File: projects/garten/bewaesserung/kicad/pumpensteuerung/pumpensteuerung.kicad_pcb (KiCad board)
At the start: 2 copper layers, 100 x 85 mm, 26 parts, among them J1 Screw_Terminal_01x03, J2 Screw_Terminal_01x02, J4 Screw_Terminal_01x03, J5 Screw_Terminal_01x03, K2 SANYOU_SRD_Form_C, K3 SANYOU_SRD_Form_C, K4 SANYOU_SRD_Form_C, Q1 2N3904, Q2 2N3904, Q3 2N3904

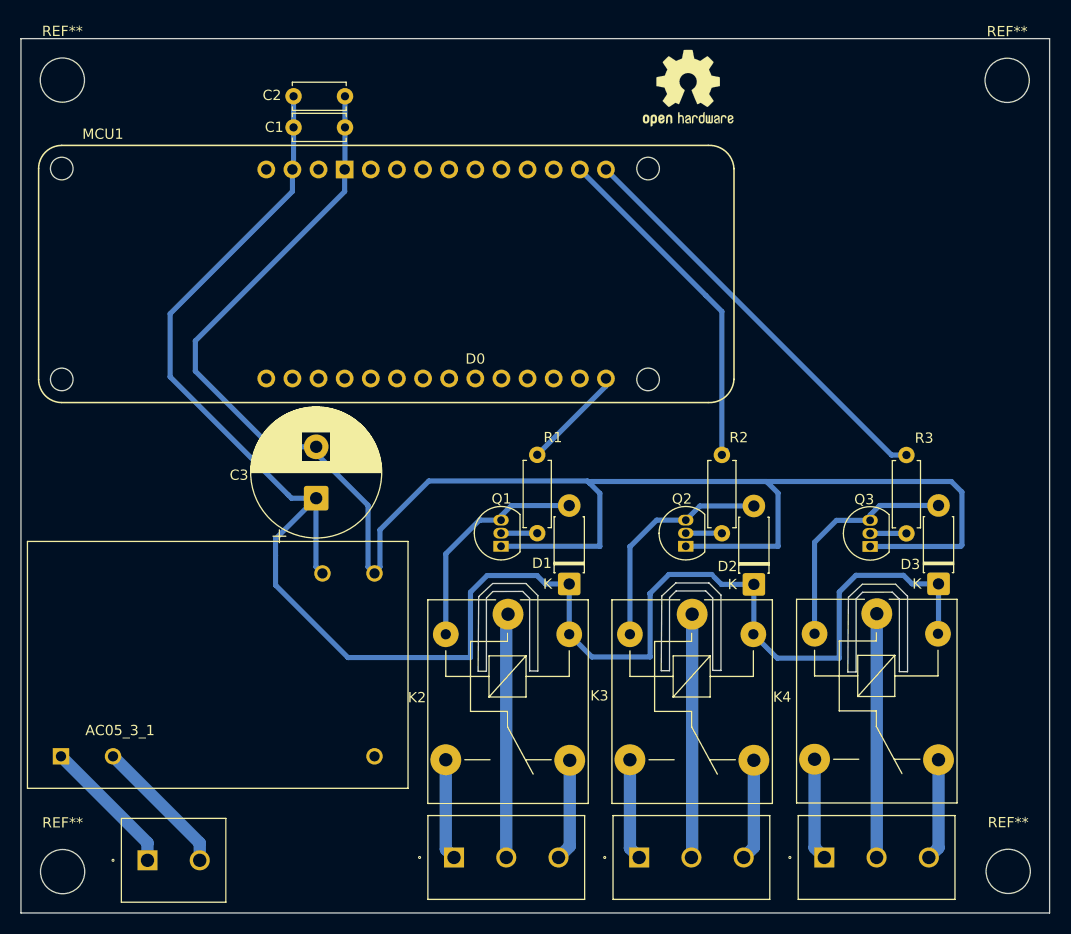
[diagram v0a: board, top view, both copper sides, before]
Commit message: [garten/bewaesserung] change powersupply from 230VAC to 24VDC
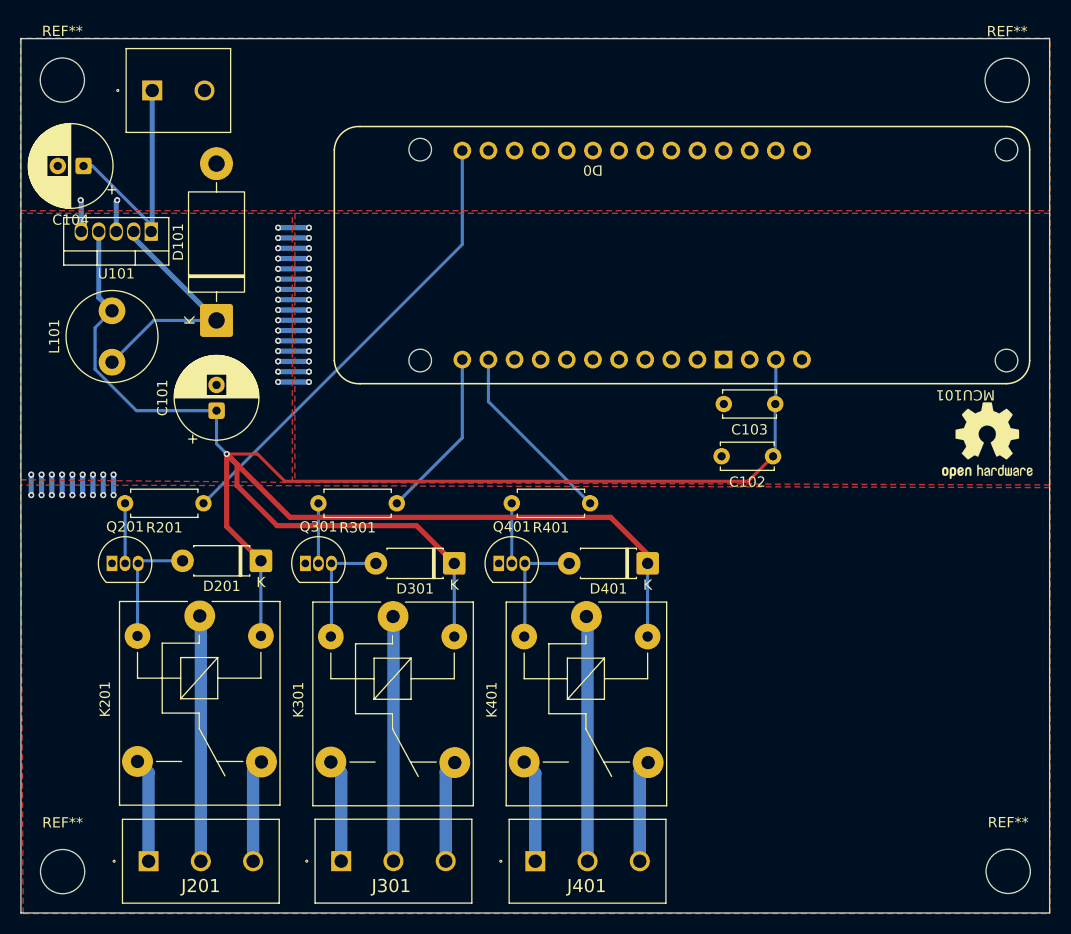
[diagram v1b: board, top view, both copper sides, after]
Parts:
- removed AC05_3_1: ~, AZFootprints:AZ_PSU_Module
- removed C1: 10000pF 100V 10% Y5P 5mm, Capacitor_THT:C_Disc_D5.0mm_W2.5mm_P5.00mm
- removed C2: 0.1uF 500V +80/-20%, Capacitor_THT:C_Disc_D5.0mm_W2.5mm_P5.00mm
- removed C3: 1000 µF, 25 V, 105°C, low ESR, 12,5 x 20 mm, RM 5, Capacitor_THT:CP_Radial_D12.5mm_P5.00mm
- removed D1, D2, D3: 1N4007, Diode_THT:D_DO-41_SOD81_P7.62mm_Horizontal
- removed J1, J4, J5: Screw_Terminal_01x03, PhoenixContact:MKDSN 1,5_3-5,08
- removed J2: Screw_Terminal_01x02, PhoenixContact:MKDSN 1,5_2-5,08
- removed K2, K3, K4: SANYOU_SRD_Form_C, Relay_THT:Relay_SPDT_SANYOU_SRD_Series_Form_C
- removed MCU1: Arduino_MKR_WAN_1310_Socket, PCM_arduino-library:Arduino_MKR_FOX_1200_Socket
- removed Q1, Q2, Q3: 2N3904, Package_TO_SOT_THT:TO-92_Inline
- removed R1, R2, R3: 220 OHM 0.6W 1% AXIAL, Resistor_THT:R_Axial_DIN0207_L6.3mm_D2.5mm_P7.62mm_Horizontal
- added C101: 330µF, Capacitor_THT:CP_Radial_D8.0mm_P2.50mm, F.Cu at (69.5, 85.2)
- added C102: 0.1uF 500V +80/-20%, Capacitor_THT:C_Disc_D5.0mm_W2.5mm_P5.00mm, F.Cu at (123.6, 89.6)
- added C103: 10000pF 100V 10% Y5P 5mm, Capacitor_THT:C_Disc_D5.0mm_W2.5mm_P5.00mm, F.Cu at (123.8, 84.5)
- added C104: 330µF, Capacitor_THT:CP_Radial_D8.0mm_P2.50mm, F.Cu at (56.6, 61.4)
- added D101: 1N5822, Diode_THT:D_DO-201AD_P15.24mm_Horizontal, F.Cu at (69.5, 76.4)
- added D201: 1N4007, Diode_THT:D_DO-41_SOD81_P7.62mm_Horizontal, F.Cu at (73.8, 99.8)
- added D301: 1N4007, Diode_THT:D_DO-41_SOD81_P7.62mm_Horizontal, F.Cu at (92.6, 100.0)
- added D401: 1N4007, Diode_THT:D_DO-41_SOD81_P7.62mm_Horizontal, F.Cu at (111.4, 100.0)
- added J101: Screw_Terminal_01x02, PhoenixContact:MKDSN 1,5_2-5,08, F.Cu at (63.3, 54.0)
- added J201: Screw_Terminal_01x03, PhoenixContact:MKDSN 1,5_3-5,08, F.Cu at (62.9, 129.0)
- added J301: Screw_Terminal_01x03, PhoenixContact:MKDSN 1,5_3-5,08, F.Cu at (81.6, 129.0)
- added J401: Screw_Terminal_01x03, PhoenixContact:MKDSN 1,5_3-5,08, F.Cu at (100.5, 129.0)
- added K201: SANYOU_SRD_Form_C, Relay_THT:Relay_SPDT_SANYOU_SRD_Series_Form_C, F.Cu at (67.9, 105.1)
- added K301: SANYOU_SRD_Form_C, Relay_THT:Relay_SPDT_SANYOU_SRD_Series_Form_C, F.Cu at (86.7, 105.2)
- added K401: SANYOU_SRD_Form_C, Relay_THT:Relay_SPDT_SANYOU_SRD_Series_Form_C, F.Cu at (105.5, 105.2)
- added L101: 330µH, Inductor_THT:L_Radial_D8.7mm_P5.00mm_Fastron_07HCP, F.Cu at (59.4, 80.5)
- added MCU101: Arduino_MKR_WAN_1310_Socket, PCM_arduino-library:Arduino_MKR_FOX_1200_Socket, F.Cu at (146.3, 80.3)
- added Q201: 2N3904, Package_TO_SOT_THT:TO-92_Inline, F.Cu at (59.4, 100.0)
- added Q301: 2N3904, Package_TO_SOT_THT:TO-92_Inline, F.Cu at (78.1, 100.0)
- added Q401: 2N3904, Package_TO_SOT_THT:TO-92_Inline, F.Cu at (96.9, 100.0)
- added R201: 1K OHM 1/2W 1% AXIAL, Resistor_THT:R_Axial_DIN0207_L6.3mm_D2.5mm_P7.62mm_Horizontal, F.Cu at (68.2, 94.2)
- added R301: 1K OHM 1/2W 1% AXIAL, Resistor_THT:R_Axial_DIN0207_L6.3mm_D2.5mm_P7.62mm_Horizontal, F.Cu at (87.0, 94.2)
- added R401: 1K OHM 1/2W 1% AXIAL, Resistor_THT:R_Axial_DIN0207_L6.3mm_D2.5mm_P7.62mm_Horizontal, F.Cu at (105.8, 94.2)
- added U101: LM2575-5.0BT, Package_TO_SOT_THT:TO-220-5_Vertical, F.Cu at (63.2, 67.8)
- moved REF** 44.9 mm to (144.4, 88.1)
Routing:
- net /-5V: track 175.4 -> 0.00 mm
- net GND: track 14.0 -> 72.2 mm, vias 0 -> 52
- net /Hauptrelais: track 10.2 -> 44.7 mm
- net /+5V: track 177.2 -> 204.4 mm, vias 0 -> 1
- net Net-(D101-K): track 0.00 -> 24.1 mm
- net Net-(D3-A): track 22.8 -> 0.00 mm
- net /Poolrelais: track 40.7 -> 18.1 mm
- net Net-(D2-A): track 22.2 -> 0.00 mm
- net Net-(D1-A): track 22.0 -> 0.00 mm
- net /Bewaesserungsrelais: track 34.1 -> 16.6 mm
- net Net-(D201-A): track 0.00 -> 11.5 mm
- net Net-(D401-A): track 0.00 -> 11.5 mm
- net Net-(D301-A): track 0.00 -> 11.5 mm
- net VCC: track 14.0 -> 23.3 mm
- net Net-(Q401-B): track 0.00 -> 5.84 mm
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- added copper zone on F.Cu, net GND
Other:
- outline, holes or cut-outs redrawn

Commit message: [garten/bewaesserung(pcb)] add another realy to disable poolfilling
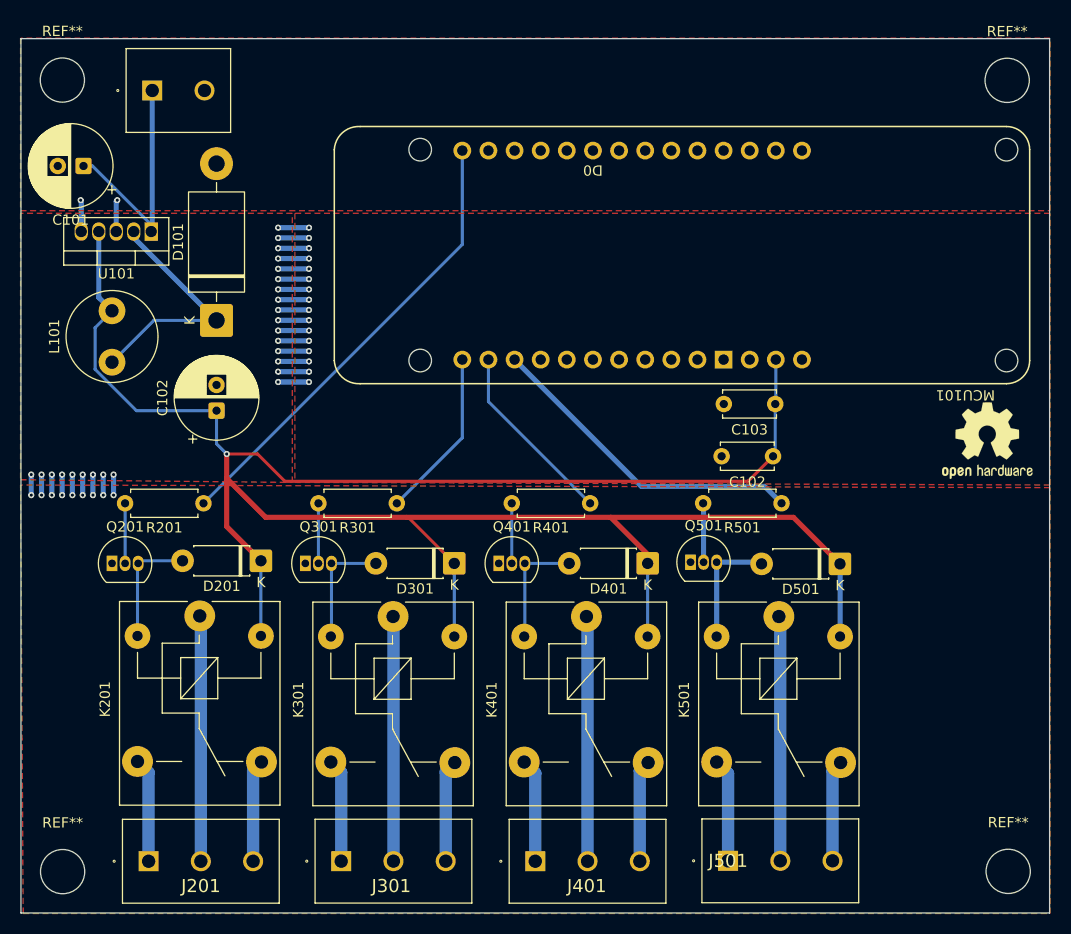
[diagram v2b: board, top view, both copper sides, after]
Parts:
- added D501: 1N4007, Diode_THT:D_DO-41_SOD81_P7.62mm_Horizontal, F.Cu at (130.1, 100.1)
- added J501: Screw_Terminal_01x03, PhoenixContact:MKDSN 1,5_3-5,08, F.Cu at (119.2, 128.9)
- added K501: SANYOU_SRD_Form_C, Relay_THT:Relay_SPDT_SANYOU_SRD_Series_Form_C, F.Cu at (124.2, 105.2)
- added Q501: 2N3904, Package_TO_SOT_THT:TO-92_Inline, F.Cu at (115.6, 99.9)
- added R501: 1K OHM 1/2W 1% AXIAL, Resistor_THT:R_Axial_DIN0207_L6.3mm_D2.5mm_P7.62mm_Horizontal, F.Cu at (124.4, 94.2)
- C101: renamed from C104; value 330µF -> 10000pF 100V 10% Y5P 5mm
- C102: value 0.1uF 500V +80/-20% -> 330µF
- C103: value 10000pF 100V 10% Y5P 5mm -> 0.1uF 500V +80/-20%
- renumbered C101 to C102
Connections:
- C101 pad 1: VCC -> /+5V
- C102 pad 1: /+5V -> VCC
- MCU101 pad D8: unconnected-(MCU101-D8_MOSI-PadD8) -> /Poolvollrelais
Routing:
- net /Poolvollrelais: track 0.00 -> 31.7 mm
- net /Poolvollrelais/IN: track 0.00 -> 23.8 mm
- net Net-(D501-A): track 0.00 -> 11.7 mm
- net /Poolvollrelais/ON: track 0.00 -> 10.1 mm
- net /Poolvollrelais/NO: track 0.00 -> 9.87 mm
- net /+5V: track 204.4 -> 213.3 mm
- net Net-(Q501-B): track 0.00 -> 5.75 mm

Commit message: [garten/bewaesserung(pcb)] move relays a littlebit more into center
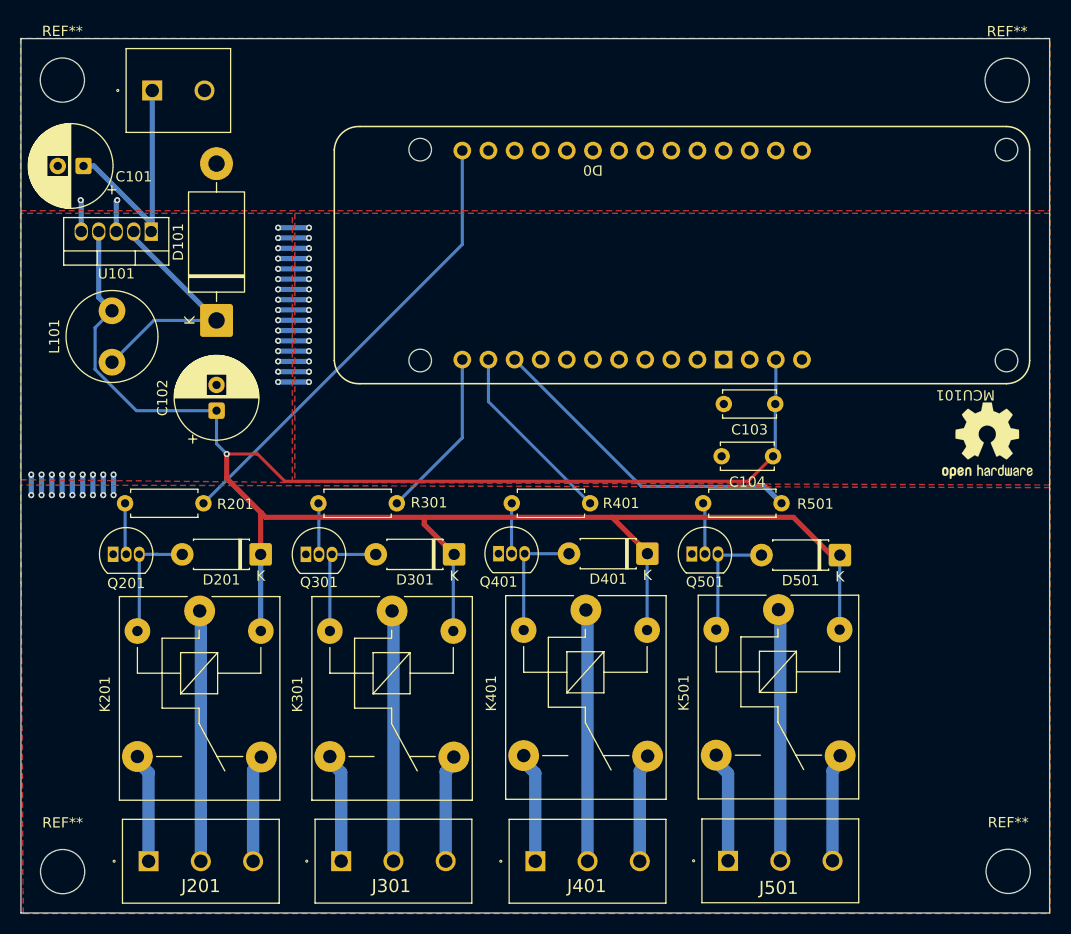
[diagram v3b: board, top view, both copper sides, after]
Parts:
- C101: value 10000pF 100V 10% Y5P 5mm -> 330µF
- C104: renamed from C102; value 330µF -> 10000pF 100V 10% Y5P 5mm
- moved D401 0.95 mm to (111.4, 99.1)
- moved Q401 0.95 mm to (96.9, 99.1)
- moved Q201 0.89 mm to (59.5, 99.1)
- moved Q301 0.88 mm to (78.2, 99.1)
- moved D301 0.88 mm to (92.6, 99.1)
- moved D501 0.85 mm to (130.1, 99.2)
- moved Q501 0.81 mm to (115.7, 99.1)
- moved K501 0.67 mm to (124.1, 104.5)
- moved K401 0.63 mm to (105.4, 104.5)
- moved D201 0.62 mm to (73.8, 99.1)
- moved K301 0.55 mm to (86.6, 104.6)
- moved K201 0.48 mm to (67.9, 104.6)
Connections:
- C101 pad 1: /+5V -> VCC
- C102 pad 1: VCC -> /+5V
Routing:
- net /+5V: track 213.3 -> 206.9 mm
- net Net-(Q401-B): track 5.84 -> 4.90 mm
- net Net-(D401-A): track 11.5 -> 12.4 mm
- net Net-(Q301-B): track 5.84 -> 4.99 mm
- net Net-(Q201-B): track 5.84 -> 5.00 mm
- net Net-(D301-A): track 11.5 -> 12.3 mm
- net Net-(Q501-B): track 5.75 -> 5.00 mm
- net /Poolvollrelais/IN: track 23.8 -> 24.5 mm
- net /Poolvollrelais/ON: track 10.1 -> 10.7 mm
- net /Poolvollrelais/NO: track 9.87 -> 10.5 mm
- net /Poolrelais/IN: track 23.8 -> 24.5 mm
- net /Poolrelais/ON: track 10.1 -> 10.7 mm
- net /Poolrelais/NO: track 9.93 -> 10.6 mm
- net VCC: track 23.3 -> 23.9 mm
- net /Bewaesserungsrelais/ON: track 10.1 -> 10.6 mm
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
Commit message: [garten/bewaesserung(pcb)] add desgin in kicad logo
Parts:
- added REF**: KiCad-Logo2_5mm_SilkScreen, Symbol:KiCad-Logo2_5mm_SilkScreen, F.Cu at (146.7, 117.1)
- moved REF** 2.25 mm to (145.9, 89.8), turned to 90 degrees

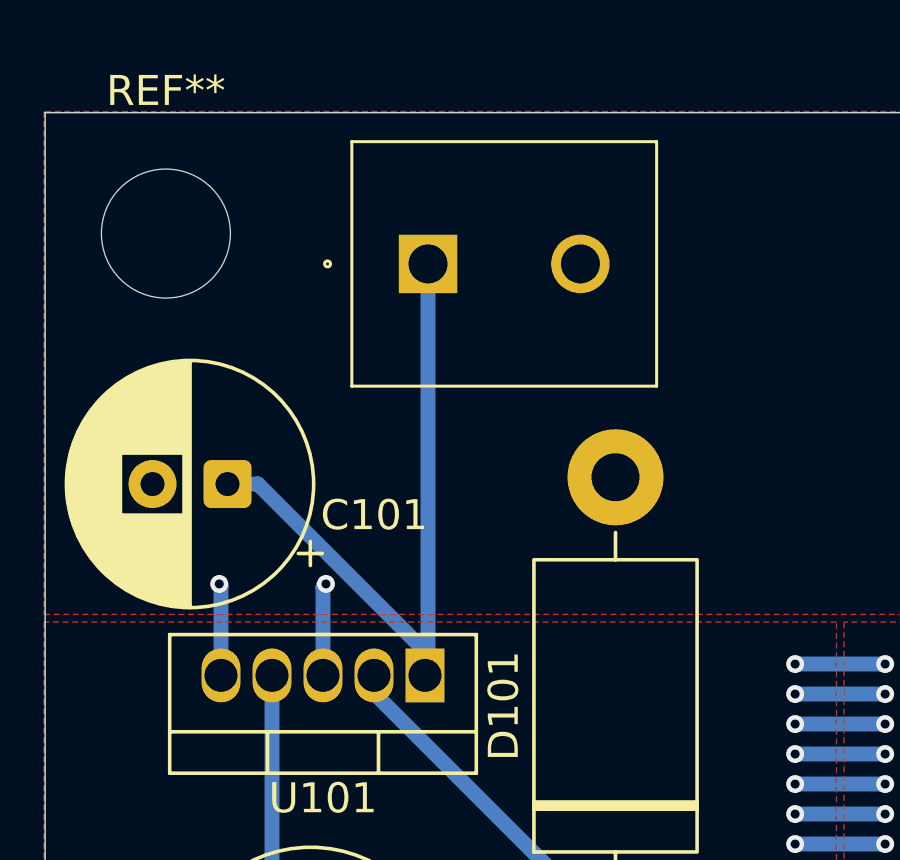
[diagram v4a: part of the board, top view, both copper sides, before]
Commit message: [garten/bewaesserung(pcb)] rotate powersupply connector
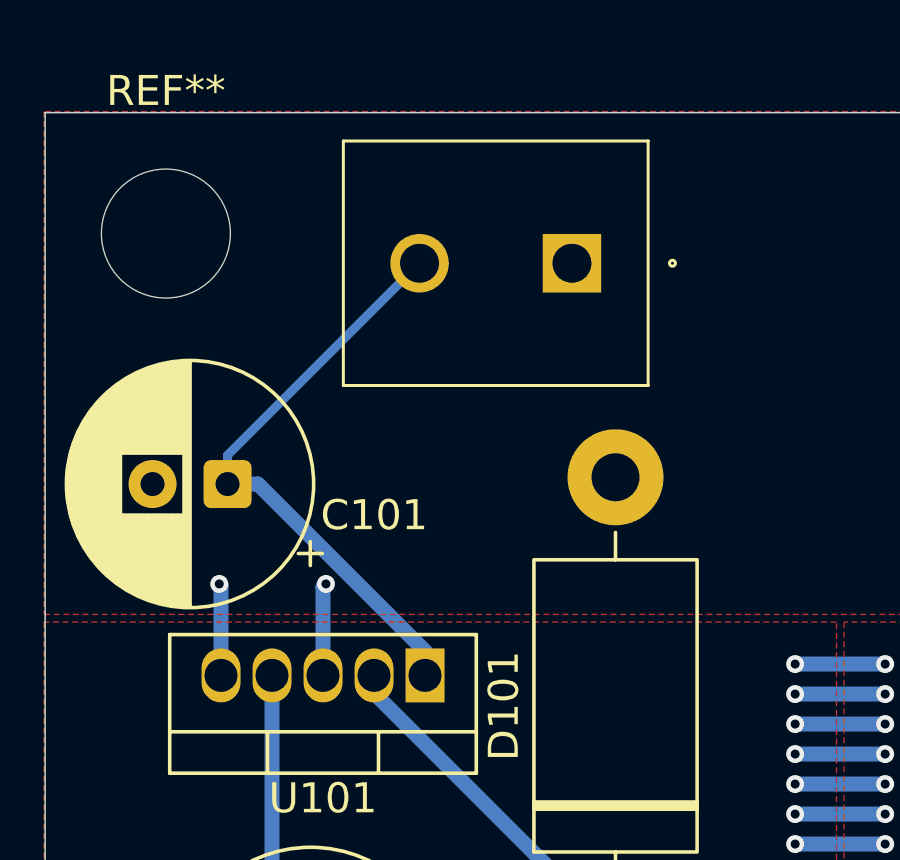
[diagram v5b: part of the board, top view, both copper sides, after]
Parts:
- moved J101 4.80 mm to (68.1, 54.0), turned to 180 degrees
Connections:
- J101 pad 1: VCC -> GND
- J101 pad 2: GND -> VCC
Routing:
- net VCC: track 23.9 -> 20.3 mm
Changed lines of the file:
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@@
 	)
 	(paper "A4")
+	(title_block
+		(date "2026-03-09")
+		(rev "5")
+		(comment 4 "AISLER Project ID: FHAAEEKF")
+	)
 	(layers
 		(0 "F.Cu" signal)
@@
 	(footprint "PhoenixContact:MKDSN 1,5_2-5,08"
 		(layer "F.Cu")
-		(at 63.263 54.042)
+		(at 68.06 54.02 180)
 		(descr "1729128")
 		(tags "Connector")
@@
 		)
 		(property "MPN" "1729128"
-			(at 0 0 0)
+			(at 0 0 180)
 			(unlocked yes)
 			(layer "F.Fab")
@@
 		(attr through_hole)
 		(fp_line
-			(start -2.54 -4.075)
-			(end 7.62 -4.075)
+			(start 7.62 4.075)
+			(end -2.54 4.075)
 			(stroke
 				(width 0.1)
@@
 		)
 		(fp_line
-			(start -2.54 4.075)
-			(end -2.54 -4.075)
+			(start 7.62 -4.075)
+			(end 7.62 4.075)
 			(stroke
 				(width 0.1)
@@
 		)
 		(fp_line
-			(start 7.62 -4.075)
-			(end 7.62 4.075)
+			(start -2.54 4.075)
+			(end -2.54 -4.075)
 			(stroke
 				(width 0.1)
@@
 		)
 		(fp_line
-			(start 7.62 4.075)
-			(end -2.54 4.075)
+			(start -2.54 -4.075)
+			(end 7.62 -4.075)
 			(stroke
 				(width 0.1)
@@
 		)
 		(fp_line
-			(start -4.25 -5.075)
-			(end 8.62 -5.075)
+			(start 8.62 5.075)
+			(end -4.25 5.075)
 			(stroke
 				(width 0.05)
@@
 		)
 		(fp_line
-			(start -4.25 5.075)
-			(end -4.25 -5.075)
+			(start 8.62 -5.075)
+			(end 8.62 5.075)
 			(stroke
 				(width 0.05)
@@
 		)
 		(fp_line
-			(start 8.62 -5.075)
-			(end 8.62 5.075)
+			(start -4.25 5.075)
+			(end -4.25 -5.075)
 			(stroke
 				(width 0.05)
@@
 		)
 		(fp_line
-			(start 8.62 5.075)
-			(end -4.25 5.075)
+			(start -4.25 -5.075)
+			(end 8.62 -5.075)
 			(stroke
 				(width 0.05)
@@
 		)
 		(fp_line
-			(start -2.54 -4.075)
-			(end 7.62 -4.075)
+			(start 7.62 4.075)
+			(end -2.54 4.075)
 			(stroke
 				(width 0.2)
@@
 		)
 		(fp_line
-			(start -2.54 4.075)
-			(end -2.54 -4.075)
+			(start 7.62 -4.075)
+			(end 7.62 4.075)
 			(stroke
 				(width 0.2)
@@
 		)
 		(fp_line
-			(start 7.62 -4.075)
-			(end 7.62 4.075)
+			(start -2.54 4.075)
+			(end -2.54 -4.075)
 			(stroke
 				(width 0.2)
@@
 		)
 		(fp_line
-			(start 7.62 4.075)
-			(end -2.54 4.075)
+			(start -2.54 -4.075)
+			(end 7.62 -4.075)
 			(stroke
 				(width 0.2)
@@
 		)
 		(pad "1" thru_hole rect
-			(at 0 0)
+			(at 0 0 180)
 			(size 1.95 1.95)
 			(drill 1.3)
 			(layers "*.Cu" "*.Mask")
 			(remove_unused_layers no)
-			(net 6 "VCC")
+			(net 7 "GND")
 			(pinfunction "Pin_1")
 			(pintype "passive")
 		)
 		(pad "2" thru_hole circle
-			(at 5.08 0)
+			(at 5.08 0 180)
 			(size 1.95 1.95)
 			(drill 1.3)
 			(layers "*.Cu" "*.Mask")
 			(remove_unused_layers no)
-			(net 7 "GND")
+			(net 6 "VCC")
 			(pinfunction "Pin_2")
 			(pintype "passive")
@@
 	)
 	(segment
-		(start 63.263 54.042)
-		(end 63.263 67.657)
-		(width 0.5)
+		(start 56.58 60.42)
+		(end 56.58 61.38)
+		(width 0.3)
+		(layer "B.Cu")
+		(net 6)
+	)
+	(segment
+		(start 62.98 54.02)
+		(end 56.58 60.42)
+		(width 0.3)
 		(layer "B.Cu")
 		(net 6)
